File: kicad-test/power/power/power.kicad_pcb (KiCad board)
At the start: 2 copper layers, 22.9 x 96.5 mm, 76 parts, among them J1 GND, J10 Conn_01x04_Pin, J2 GND2, J3 +15V, J4 -15V, J5 +5V, J6 +48V, J7 USB_C_Receptacle_USB2.0_16P, J8 PH_EN, J9 USB_C_Receptacle_USB2.0_16P, T1 475uH, U18 PTN5150AHXMP, U20 TPS7A39, U21 SN6505BDBV, U22 TPS2116DRL, U23 TPS62172DSG, U25 TPS7A2009, U26 TPS62171DSG, U27 TPS7A4101, U28 TPS61391, U30 CH224K

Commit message: added test points
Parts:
- moved R121 167.3 mm to (181.6, 154.9)
- moved C161 128.0 mm to (189.6, 85.2), turned to 90 degrees
- moved U21 124.3 mm to (185.7, 85.2), turned to 90 degrees
- moved R108 120.6 mm to (181.9, 85.2), turned to -90 degrees
- moved T1 113.8 mm to (185.4, 93.3), turned to -90 degrees
- moved D64 98.6 mm to (180.3, 91.7), turned to 90 degrees
- moved C177 96.4 mm to (132.1, 41.9)
- moved C178 96.4 mm to (132.1, 44.9)
- moved C157 96.1 mm to (168.9, 134.1), turned to -90 degrees
- moved D69 95.9 mm to (177.8, 91.7), turned to -90 degrees
- moved C158 92.6 mm to (180.3, 96.5)
- moved C162 89.7 mm to (177.8, 96.5), turned to 90 degrees
- moved C176 85.1 mm to (116.8, 43.2), turned to -90 degrees
- moved U27 84.4 mm to (110.8, 43.5)
- moved R109 75.4 mm to (153.4, 137.7), turned to 0 degrees
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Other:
- board outline removed

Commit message: board footprint layout
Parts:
- removed U25: TPS7A2009, Package_SON:Texas_X2SON-4_1x1mm_P0.65mm
- added C164: 10uF, Capacitor_SMD:C_0805_2012Metric_Pad1.18x1.45mm_HandSolder, F.Cu at (179.7, 61.0)
- added C199: 1uF, Capacitor_SMD:C_0805_2012Metric_Pad1.18x1.45mm_HandSolder, F.Cu at (102.2, 52.7)
- added C200: 1uF, Capacitor_SMD:C_0805_2012Metric_Pad1.18x1.45mm_HandSolder, F.Cu at (102.2, 46.4)
- added J11: EN_15V, Connector_PinHeader_2.54mm:PinHeader_1x02_P2.54mm_Vertical, F.Cu at (127.0, 59.7)
- added J12: EN_3V3, Connector_PinHeader_2.54mm:PinHeader_1x02_P2.54mm_Vertical, F.Cu at (127.0, 46.4)
- added J13: EN_1V8_0V9, Connector_PinHeader_2.54mm:PinHeader_1x02_P2.54mm_Vertical, F.Cu at (137.8, 46.4)
- added J15: EN_0V9, Connector_PinHeader_2.54mm:PinHeader_1x02_P2.54mm_Vertical, F.Cu at (148.5, 46.4)
- added R124: 100k, Resistor_SMD:R_0805_2012Metric_Pad1.20x1.40mm_HandSolder, F.Cu at (134.0, 45.4)
- added R125: 100k, Resistor_SMD:R_0805_2012Metric_Pad1.20x1.40mm_HandSolder, F.Cu at (123.2, 45.4)
- added R126: 100k, Resistor_SMD:R_0805_2012Metric_Pad1.20x1.40mm_HandSolder, F.Cu at (153.0, 45.4)
- added TP1: PH_MID, TestPoint:TestPoint_Keystone_5010-5014_Multipurpose, F.Cu at (151.1, 79.4)
- added TP2: 15V_MID, TestPoint:TestPoint_Keystone_5010-5014_Multipurpose, F.Cu at (156.2, 65.4)
- added TP3: 5V_EXT, TestPoint:TestPoint_Keystone_5010-5014_Multipurpose, F.Cu at (102.2, 64.1)
- added TP4: 5V_PD, TestPoint:TestPoint_Keystone_5010-5014_Multipurpose, F.Cu at (102.2, 33.0)
- added TP5: 5V_MID, TestPoint:TestPoint_Keystone_5010-5014_Multipurpose, F.Cu at (112.4, 48.9)
- added U1: TPS7A2009, Package_TO_SOT_SMD:SOT-23-5, F.Cu at (148.5, 37.5)
- J8: value PH_EN -> EN_PH
- R121: value 10k -> 100k
- moved J9 100.3 mm to (94.6, 41.9), turned to -90 degrees
- moved C197 99.4 mm to (102.2, 36.8), turned to 0 degrees
- moved J2 98.3 mm to (185.4, 64.8), turned to 180 degrees
- moved R121 97.8 mm to (123.2, 76.6), turned to -90 degrees
- moved C198 96.1 mm to (102.2, 40.0), turned to 180 degrees
- moved L2 95.8 mm to (138.0, 34.0), turned to 180 degrees
- moved C168 94.6 mm to (134.6, 37.5), turned to -90 degrees
- moved C181 92.6 mm to (111.1, 38.1), turned to -90 degrees
- moved J8 92.1 mm to (127.0, 75.6)
- moved C166 90.6 mm to (123.8, 37.5), turned to -90 degrees
- moved U26 90.6 mm to (137.8, 37.5), turned to 90 degrees
- moved U30 90.5 mm to (107.3, 40.0), turned to -90 degrees
- moved R123 90.4 mm to (102.2, 43.2), turned to 180 degrees
- moved L1 89.9 mm to (127.0, 34.0), turned to 180 degrees
- moved D2 89.4 mm to (114.3, 39.4), turned to 0 degrees
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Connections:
- J8 pad 1: +3V3 -> Net-(J8-Pin_1)
- J8 pad 2: Net-(J8-Pin_2) -> +3V3
- R106 pad 2: -15V -> Net-(U20-FBN)
- R108 pad 1: Net-(U21-EN) -> Net-(J11-Pin_2)
- R109 pad 1: -15V -> Net-(U20-FBN)
- R121 pad 1: Net-(J8-Pin_2) -> Net-(J8-Pin_1)
- U20 pad 7: -15V -> Net-(U20-FBN)
- U21 pad 5: Net-(U21-EN) -> Net-(J11-Pin_1)
- U23 pad 3: +5V -> Net-(J12-Pin_1)
- U26 pad 3: +5V -> Net-(J13-Pin_1)
- U28 pad 13: Net-(J8-Pin_2) -> Net-(J8-Pin_1)
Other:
- board outline added: 100 x 61 mm
- board text added: "+5V"
- board text added: "15V_MID"
- board text added: "EN +48V"
- board text added: "EN 0V9"
- board text added: "EN 1V8"
- board text added: "EN 3V3"
- board text added: "EN ±15V"
- board text added: "PH_MID"
- board text added: "VBUS EXT"
- board text added: "VBUS PD"

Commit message: power board first draft
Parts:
- R116, R117, R122, R94: footprint Resistor_SMD:R_0603_1608Metric_Pad0.98x0.95mm_HandSolder -> Resistor_SMD:R_0805_2012Metric_Pad1.20x1.40mm_HandSolder
- turned J15 to -90 degrees
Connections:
- J7 pad A5: /CC1 -> /CC1_EXT
- J7 pad B5: /CC2 -> /CC2_EXT
- U18 pad 1: /CC1 -> /CC1_EXT
- U18 pad 2: /CC2 -> /CC2_EXT
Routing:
- net +3V3: track 0.00 -> 181.4 mm, vias 0 -> 3
- net +5V: track 0.00 -> 78.2 mm
- net +1V8: track 0.00 -> 76.4 mm
- net +0V9: track 0.00 -> 43.7 mm
- net Net-(D61-K): track 0.00 -> 37.3 mm, vias 0 -> 2
- net /+5V_EXT: track 0.00 -> 29.2 mm
- net /VBUS: track 0.00 -> 28.1 mm
- net Net-(D64-K): track 0.00 -> 27.7 mm
- net Net-(J8-Pin_1): track 0.00 -> 19.8 mm, vias 0 -> 1
- net Net-(D69-A): track 0.00 -> 18.9 mm, vias 0 -> 2
- net /DP: track 0.00 -> 17.9 mm, vias 0 -> 2
- net /DM: track 0.00 -> 15.6 mm, vias 0 -> 2
- net Net-(U27-FB): track 0.00 -> 13.7 mm, vias 0 -> 2
- net Net-(J15-Pin_1): track 0.00 -> 12.6 mm
- net Net-(J13-Pin_1): track 0.00 -> 11.9 mm, vias 0 -> 1
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- added copper zone on F.Cu, net +15V
- added copper zone on F.Cu, net +48V
- added copper zone on F.Cu, net +5V
- added copper zone on F.Cu, net -15V
- added copper zone on B.Cu, net Earth
- added copper zone on F.Cu, net Earth

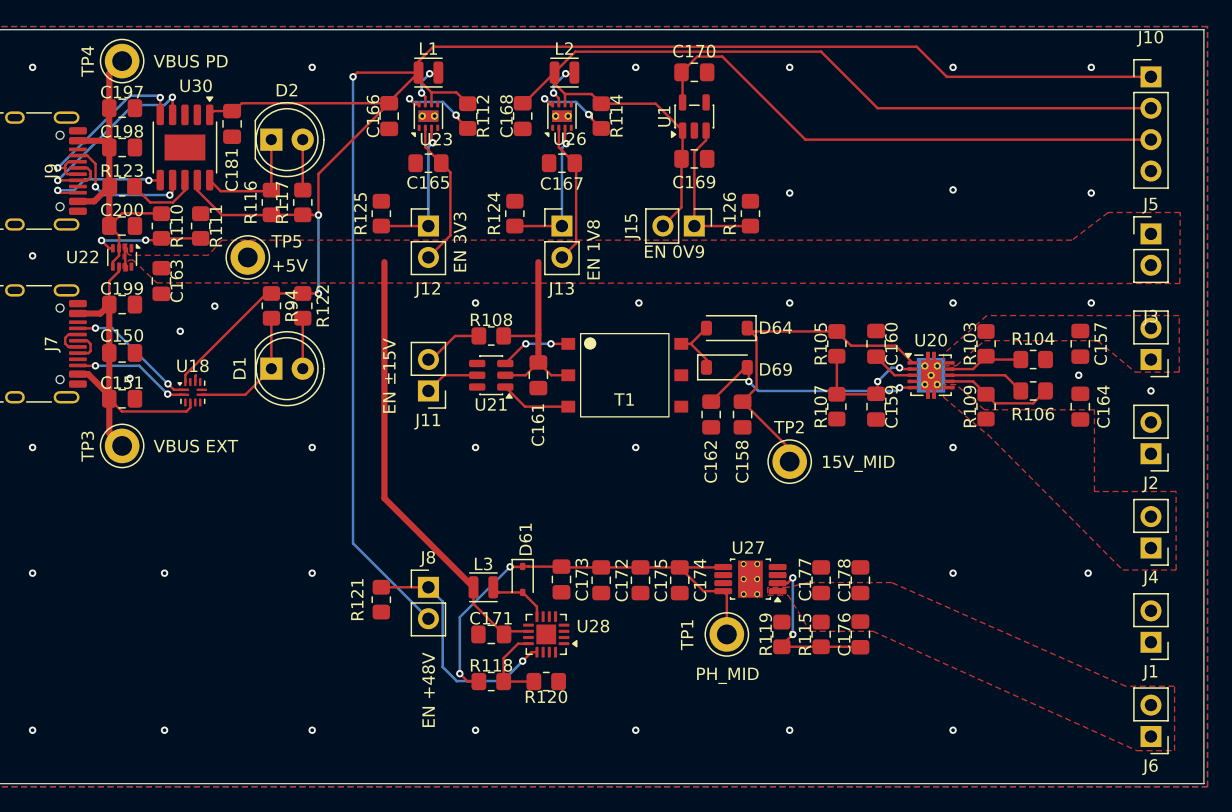
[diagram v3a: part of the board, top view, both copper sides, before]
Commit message: trace widths
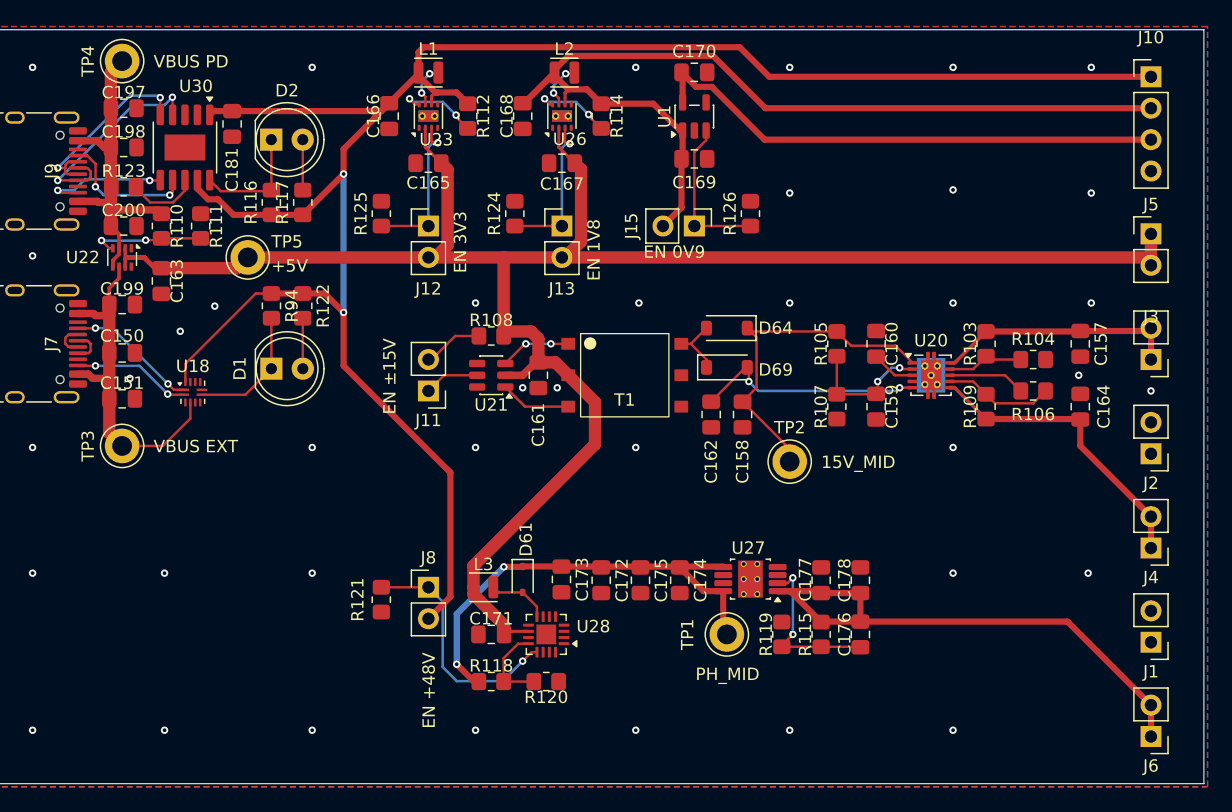
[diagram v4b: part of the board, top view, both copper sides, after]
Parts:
- moved C197 0.13 mm to (102.4, 36.8)
- moved C198 0.13 mm to (102.4, 40.0)
- moved C200 0.13 mm to (102.4, 46.4)
- moved R123 0.13 mm to (102.4, 43.2)
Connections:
- net Net-(D61-K) renamed /PH_MID
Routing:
- net +5V: track 78.2 -> 158.8 mm
- net +48V: track 0.00 -> 45.6 mm
- net -15V: track 0.00 -> 24.7 mm
- net +15V: track 0.00 -> 20.0 mm
- net +3V3: track 181.4 -> 165.9 mm, vias 3 -> 2
- net +0V9: track 43.7 -> 42.7 mm
- net Net-(J12-Pin_1): track 11.9 -> 12.8 mm
- net /+5V_EXT: track 29.2 -> 28.6 mm
- net Earth: track 0.57 -> 0.00 mm, vias 37 -> 39
- net Net-(J13-Pin_1): track 11.9 -> 12.5 mm
- removed copper zone on F.Cu, net +15V
- removed copper zone on F.Cu, net +48V
- removed copper zone on F.Cu, net +5V
- removed copper zone on F.Cu, net -15V

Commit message: bom update
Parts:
- D4: renamed from D2; footprint LED_THT:LED_D5.0mm -> LED_SMD:LED_0805_2012Metric_Pad1.15x1.40mm_HandSolder
- D5: renamed from D1; footprint LED_THT:LED_D5.0mm -> LED_SMD:LED_0805_2012Metric_Pad1.15x1.40mm_HandSolder
- L2: renamed from L1; footprint Inductor_SMD:L_Wuerth_PMCI-201610 -> Inductor_SMD_Wurth:L_Wurth_WE-LQSH-3012
- L3: renamed from L2; footprint Inductor_SMD:L_Wuerth_PMCI-201610 -> Inductor_SMD_Wurth:L_Wurth_WE-LQSH-3012
- moved D4 1.33 mm to (115.6, 39.3)
- moved D5 1.26 mm to (115.6, 57.9)
- renumbered C161 to C1, C162 to C10, C169 to C11, C159 to C12, C174 to C13, C170 to C14, C175 to C15, C160 to C16, C176 to C17, C157 to C18, C164 to C19, C165 to C2, C177 to C20, C178 to C21, C181 to C22, C150 to C23, C197 to C24, C151 to C25, C198 to C26, C200 to C27, C199 to C28, C163 to C29, C167 to C3, C171 to C4, C172 to C5, C166 to C6, C168 to C7, C173 to C8, C158 to C9, D61 to D1, D64 to D2, D69 to D3, J12 to J1, J1 to J10, J10 to J11, J2 to J12, J9 to J13, J7 to J14, J13 to J2, J8 to J3, J11 to J4, J15 to J5, J3 to J6, J4 to J7, J5 to J8, J6 to J9, L3 to L1, R125 to R1, R105 to R10, R107 to R11, R106 to R12, R103 to R13, R109 to R14, R104 to R15, R115 to R16, R119 to R17, R117 to R18, R116 to R19, R124 to R2, R123 to R20, R122 to R21, R110 to R22, R111 to R23, R94 to R24, R121 to R3, R108 to R4, R112 to R5, R114 to R6, R118 to R7, R120 to R8, R126 to R9, TP4 to TP3, TP3 to TP4, U23 to U1, U22 to U10, U26 to U2, U21 to U3, U28 to U4, U1 to U5, U20 to U6, U27 to U7, U30 to U8, U18 to U9
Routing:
- net Net-(U2-SW): track 3.80 -> 5.74 mm
- net Net-(U1-SW): track 3.60 -> 5.26 mm
- net +3V3: track 165.9 -> 166.7 mm
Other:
- board text added: "+0V9"
- board text added: "+15V"
- board text added: "+1V8"
- board text added: "+3V3"
- board text added: "+48V"
- board text added: "-15V"
- board text added: "GND"

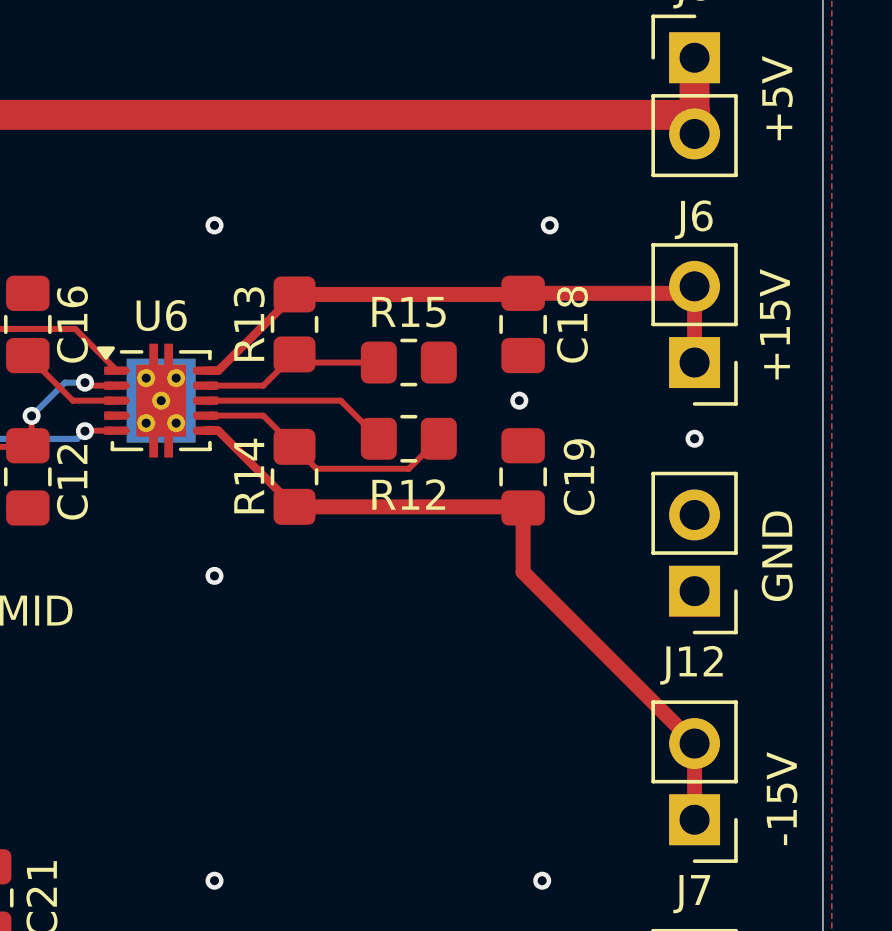
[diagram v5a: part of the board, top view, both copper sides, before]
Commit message: standard jlc resistor values
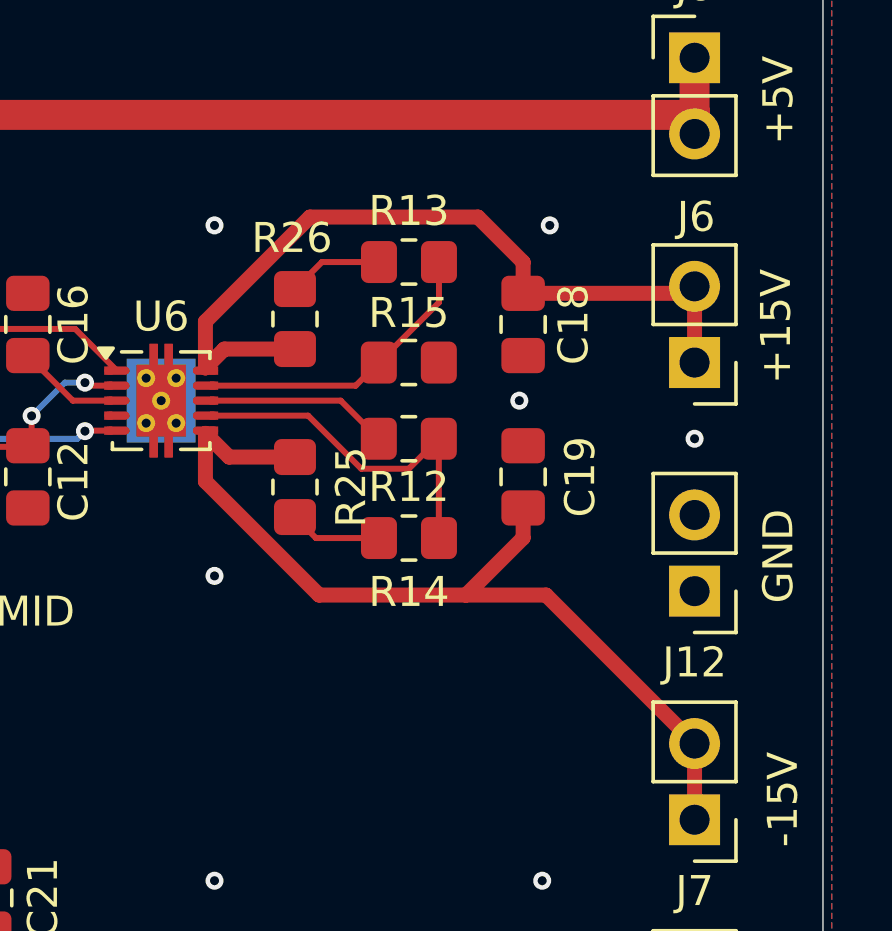
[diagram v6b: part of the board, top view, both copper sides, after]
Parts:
- added R25: 27k, Resistor_SMD:R_0805_2012Metric_Pad1.20x1.40mm_HandSolder, F.Cu at (172.1, 61.3)
- added R26: 100k, Resistor_SMD:R_0805_2012Metric_Pad1.20x1.40mm_HandSolder, F.Cu at (172.1, 55.7)
- R10: value 499k -> 470
- R13: value 118k -> 20k
- R14: value 127k -> 100k
- moved R13 4.35 mm to (175.9, 53.8), turned to 0 degrees
- moved R14 4.33 mm to (175.9, 63.0), turned to 180 degrees
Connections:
- R13 pad 1: +15V -> Net-(R13-Pad1)
- R14 pad 2: -15V -> Net-(R14-Pad2)
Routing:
- net +15V: track 20.0 -> 26.8 mm
- net -15V: track 24.7 -> 31.4 mm
- net Net-(U6-FBP): track 6.32 -> 10.3 mm
- net Net-(U6-FBN): track 8.93 -> 12.2 mm
- net Net-(R13-Pad1): track 0.00 -> 3.17 mm
- net Net-(R14-Pad2): track 0.00 -> 3.09 mm

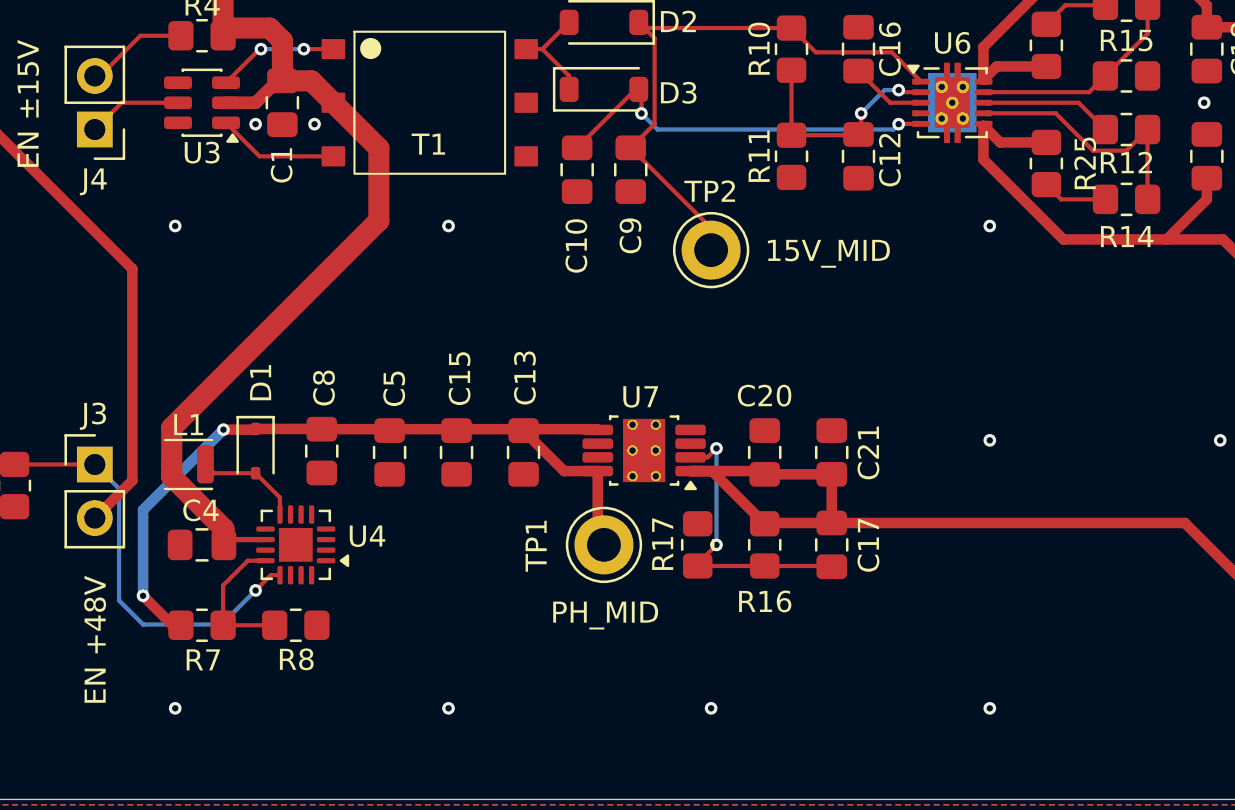
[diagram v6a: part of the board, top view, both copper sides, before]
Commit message: add JLC and MPN to BOM
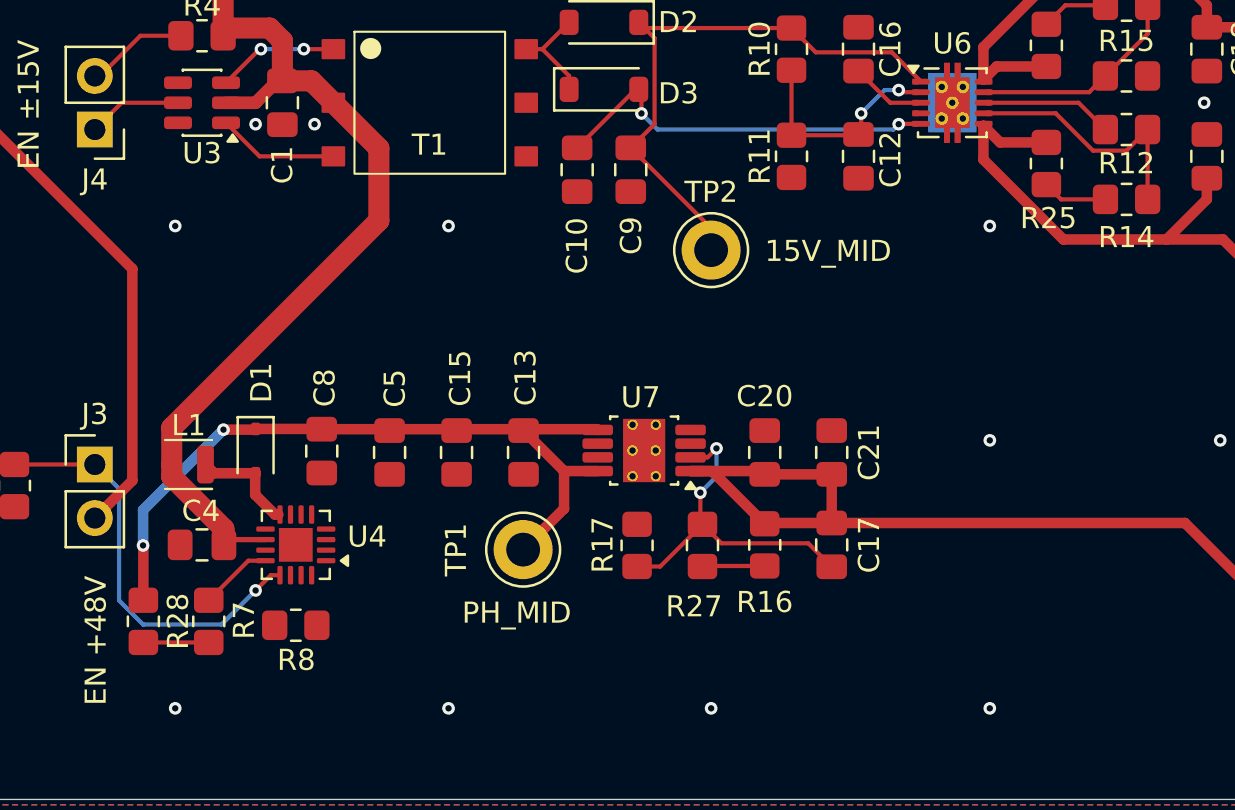
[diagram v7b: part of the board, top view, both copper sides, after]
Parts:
- added R27: 200k, Resistor_SMD:R_0805_2012Metric_Pad1.20x1.40mm_HandSolder, F.Cu at (155.8, 79.4)
- added R28: 200k, Resistor_SMD:R_0805_2012Metric_Pad1.20x1.40mm_HandSolder, F.Cu at (129.3, 83.0)
- R16: value 475k -> 200k
- R17: value 12k -> 10k
- R22: value 330k -> 220k
- R23: value 100k -> 68k
- R7: value 392k -> 200k
- moved TP1 3.84 mm to (147.3, 79.6)
- moved R17 2.88 mm to (152.7, 79.4)
- moved R7 0.37 mm to (132.4, 83.0), turned to 90 degrees
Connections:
- R16 pad 2: Net-(U7-FB) -> Net-(R16-Pad2)
- R7 pad 1: /PH_MID -> Net-(R28-Pad2)
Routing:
- net Net-(U4-FB): track 6.83 -> 3.46 mm
- net Net-(R28-Pad2): track 0.00 -> 3.10 mm
- net Net-(R16-Pad2): track 0.00 -> 2.96 mm
- net Net-(U7-FB): track 13.7 -> 16.2 mm
- net /PH_MID: track 37.5 -> 36.3 mm

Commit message: power board layout updates
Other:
- board text added: "OpenMic Power board prototype v0.1 5/14/26"
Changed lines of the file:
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@@
 		(layer "Edge.Cuts")
 	)
+	(gr_text "OpenMic\nPower board prototype v0.1\n5/14/26"
+		(at 95 84.1 0)
+		(layer "F.SilkS")
+		(effects
+			(font
+				(size 1 1)
+				(thickness 0.1)
+			)
+			(justify left bottom)
+		)
+	)
 	(gr_text "VBUS PD"
 		(at 104.775 33.655 0)
@@
 	)
 	(segment
+		(start 155.825 80.375)
+		(end 155.8 80.4)
+		(width 0.2)
+		(layer "F.Cu")
+		(net "Net-(R16-Pad2)")
+	)
+	(segment
+		(start 158.75 80.375)
+		(end 155.825 80.375)
+		(width 0.2)
+		(layer "F.Cu")
+		(net "Net-(R16-Pad2)")
+	)
+	(segment
 		(start 106.088235 43.85)
 		(end 106.315 43.623235)
@@
 	)
 	(segment
+		(start 129.3 84)
+		(end 132.4 84)
+		(width 0.2)
+		(layer "F.Cu")
+		(net "Net-(R28-Pad2)")
+	)
+	(segment
 		(start 132.4 82)
 		(end 134.275 80.125)
@@
 		(net "Net-(U1-PG)")
 	)
-	(segment
-		(start 129.3 84)
-		(end 132.4 84)
-		(width 0.2)
-		(layer "F.Cu")
-		(net "Net-(R28-Pad2)")
-	)
-	(segment
-		(start 155.825 80.375)
-		(end 155.8 80.4)
-		(width 0.2)
-		(layer "F.Cu")
-		(net "Net-(R16-Pad2)")
-	)
-	(segment
-		(start 158.75 80.375)
-		(end 155.825 80.375)
-		(width 0.2)
-		(layer "F.Cu")
-		(net "Net-(R16-Pad2)")
-	)
 	(zone
